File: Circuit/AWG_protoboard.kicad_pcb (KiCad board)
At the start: 2 copper layers, 63.5 x 27.9 mm, 12 parts, among them J1 Power, J2 Pump 1, J3 Pump 2, J4 Mosfet, J5 Arduino, M1 Fan_3pin, M2 Fan_3pin, U2 LCD-016N002L

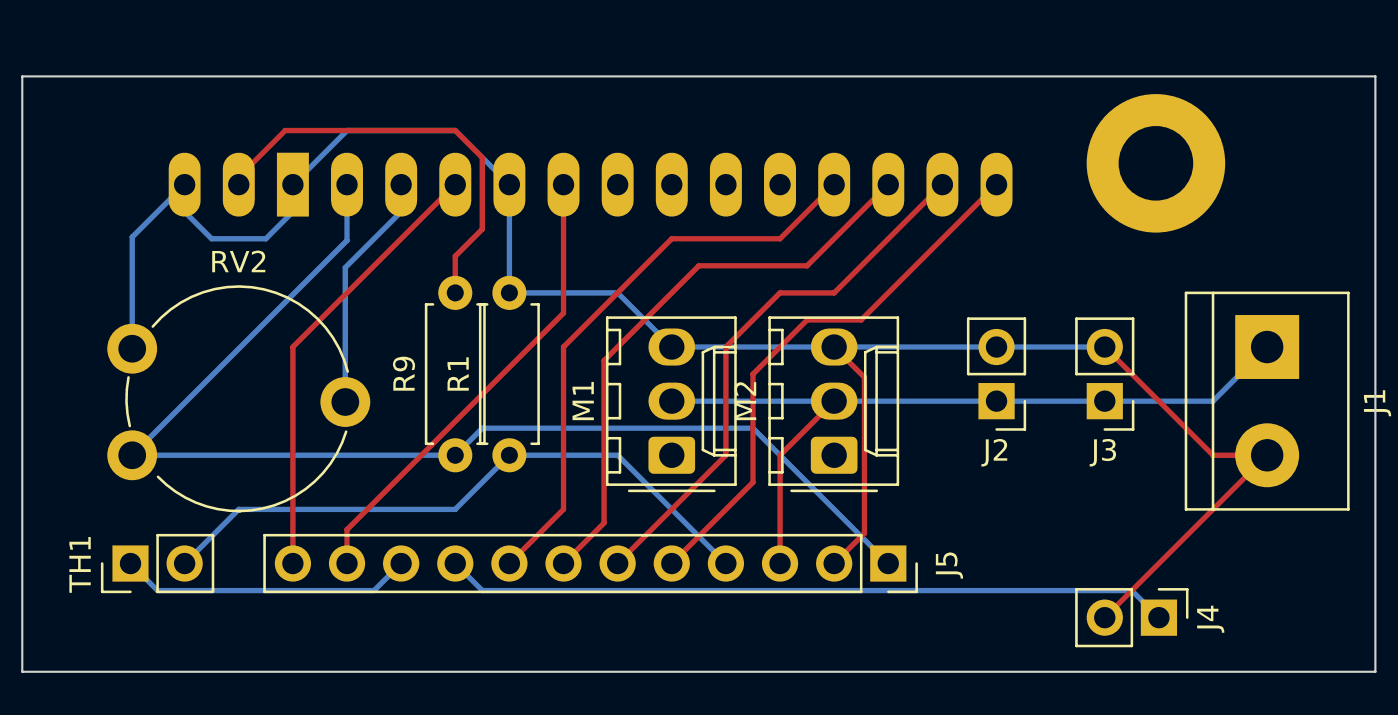
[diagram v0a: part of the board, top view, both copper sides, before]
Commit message: [Circuit] Improvements on protoboard layout
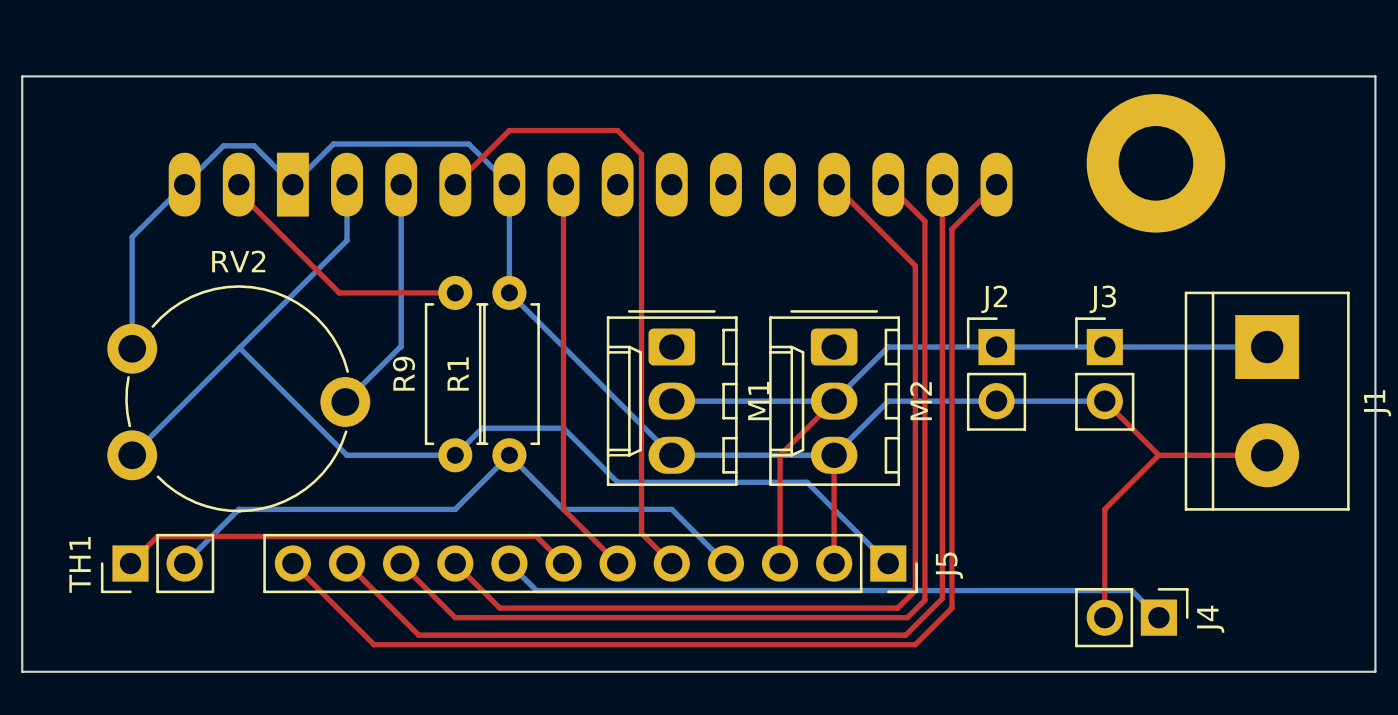
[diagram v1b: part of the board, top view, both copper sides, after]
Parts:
- moved M1 5.08 mm to (165.1, 96.5), turned to -90 degrees
- moved M2 5.08 mm to (172.7, 96.5), turned to -90 degrees
- moved J2 2.54 mm to (180.3, 96.5), turned to 0 degrees
- moved J3 2.54 mm to (185.4, 96.5), turned to 0 degrees
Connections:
- J5 pad 10: /D7 -> /D4
- J5 pad 11: /D11 -> /D3
- J5 pad 12: /D12 -> /D2
- J5 pad 5: /D2 -> /D12
- J5 pad 6: /D3 -> /D11
- J5 pad 7: /D4 -> /D7
- J5 pad 8: /D5 -> /D6
- J5 pad 9: /D6 -> /D5
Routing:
- net /D2: track 25.6 -> 54.0 mm
- net /D3: track 25.6 -> 49.5 mm
- net /D4: track 27.1 -> 46.2 mm
- net /D5: track 27.1 -> 43.4 mm
- net /D12: track 20.9 -> 30.0 mm
- net GND: track 95.6 -> 86.7 mm
- net Net-(R9-Pad2): track 20.1 -> 12.5 mm
- net /D7: track 13.8 -> 21.4 mm
- net /D11: track 22.0 -> 18.8 mm
- net +5V: track 55.5 -> 52.6 mm
- net /D6: track 34.1 -> 31.5 mm
